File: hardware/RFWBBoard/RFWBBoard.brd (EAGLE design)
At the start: 90 x 56 mm, 123 parts, among them IC1 24LC025ST, J1 CON-71742-3003-BOT, M1 MOUNT-HOLE3.3, M2 MOUNT-HOLE3.3, M3 MOUNT-HOLE3.3, M4 MOUNT-HOLE3.3, M5 FIDUCIAL1X2, M6 FIDUCIAL1X2, M7 FIDUCIAL1X2, M8 FIDUCIAL1X2, U1 MAX2830IPC-7351, U2 LDB212G4010C-001, U3 LDB212G4010C-001, U4 AD8132MSOP8, U5 AD8132MSOP8, U6 AD8132MSOP8, U7 AD8132MSOP8, U8 ICS83021I, U9 ICS85320I, X1 SMA-SMD, X2 SMA-SMD, X3 FOX924B, X4 SMA-SMD, X5 SMA-SMD, X6 SMA-SMD, X7 SMA-SMD

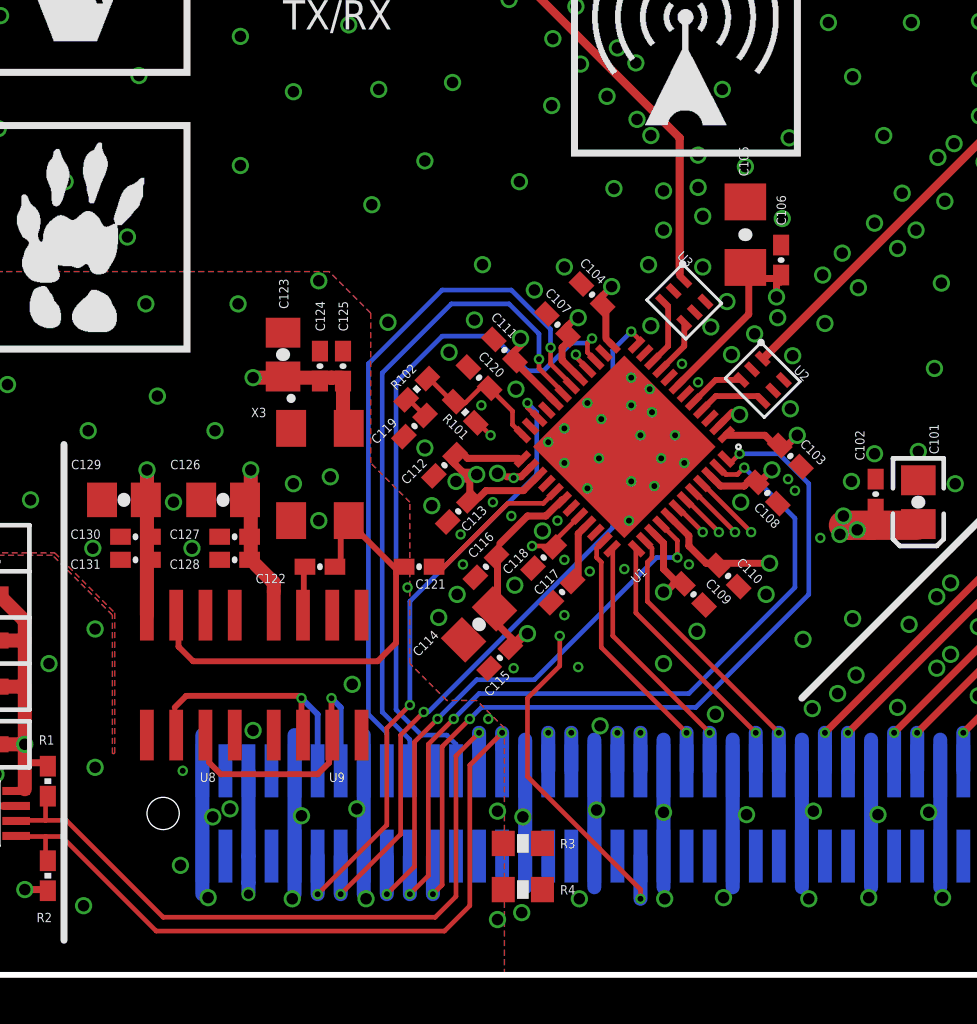
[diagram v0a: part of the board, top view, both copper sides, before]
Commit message: Errors corrected:
Radio Board

- External TCXO is connected to MAX2830 XTAL pin (28) instead of CTUNE pin (29)
- TCXO power supply digital, ground analog
- Mark for 1. pin for baluns not visible enough
- C105, C106 names covered by vias in documentation (PCB changed only)


Breakout Board

- 84 mezzanine connectors on top and bottom swapped


Power Board

- Silkscreen labels D1V5 and D3V3 are swapped
- VBUS measurement point not assembled
- SW2 name missing, needs caption (silk screen)
- Power input needs description (silk screen)
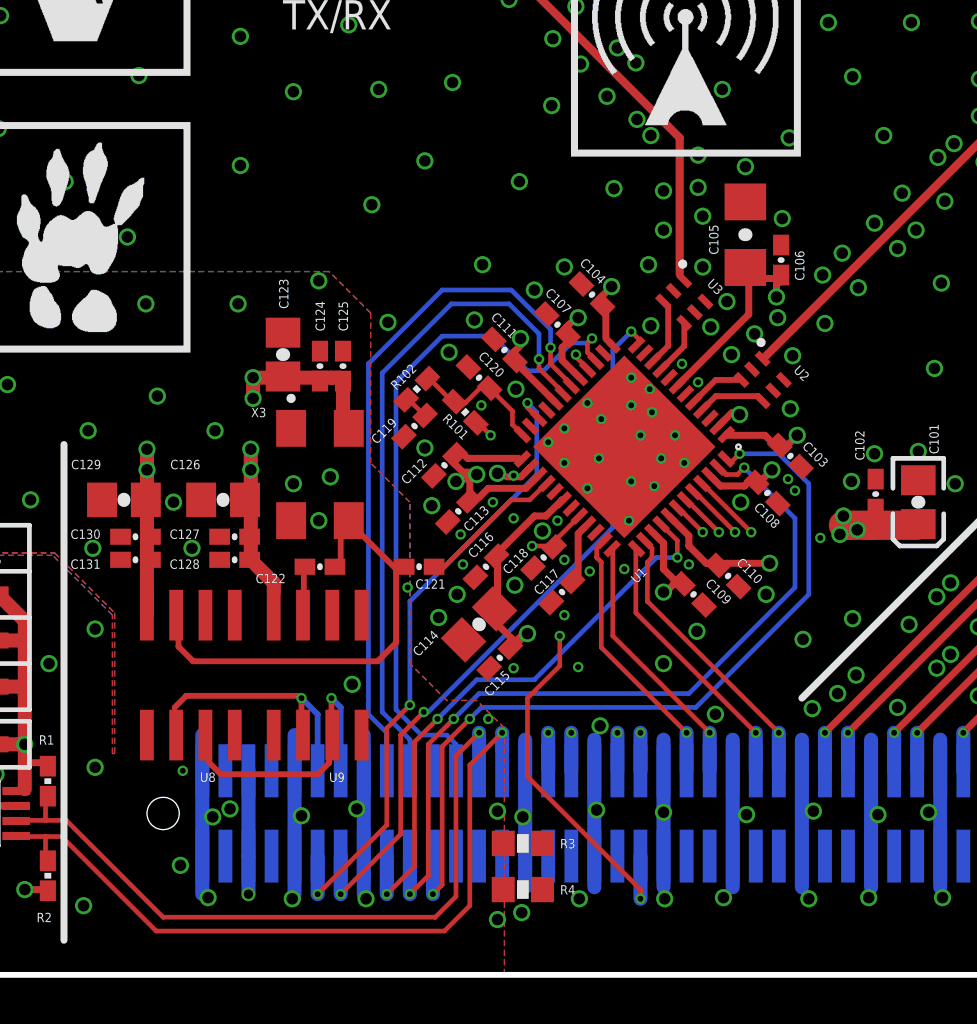
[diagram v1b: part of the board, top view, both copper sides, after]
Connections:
- net A3V3: no longer C123.1, C124.1, C125.1, C126.1, C127.1, C128.1, C129.1, C130.1, C131.1, U8.8, U9.8, X3.4
- net D3V3: now also C123.1, C124.1, C125.1, C126.1, C127.1, C128.1, C129.1, C130.1, C131.1, U8.8, U9.8, X3.4
- net N$6: now also U1.28; no longer U1.29
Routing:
- net D3V3: track 39.0 -> 81.6 mm, vias 3 -> 9
- net A3V3: track 134.4 -> 98.8 mm, vias 35 -> 32
- net DGND: vias 52 -> 51
- added copper zone on layer 15, net D3V3

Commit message: - Fiducials in both sides
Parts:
- added M10, M11, M12, M9: FIDUCIAL1X2, RFWBBoard:FIDUCIAL-1X2
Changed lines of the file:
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@@
 <grid distance="0.5" unitdist="mm" unit="mm" style="dots" multiple="1" display="yes" altdistance="0.1" altunitdist="mm" altunit="mm"/>
 <layers>
-<layer number="1" name="SIGNAL1" color="4" fill="1" visible="yes" active="yes"/>
+<layer number="1" name="SIGNAL1" color="4" fill="1" visible="no" active="yes"/>
 <layer number="2" name="GND1" color="2" fill="1" visible="no" active="yes"/>
-<layer number="3" name="SIGNAL2" color="4" fill="1" visible="yes" active="yes"/>
+<layer number="3" name="SIGNAL2" color="4" fill="1" visible="no" active="yes"/>
 <layer number="14" name="GND2" color="2" fill="1" visible="no" active="yes"/>
 <layer number="15" name="SUPPLY" color="14" fill="1" visible="no" active="yes"/>
@@
 <layer number="19" name="Unrouted" color="6" fill="1" visible="yes" active="yes"/>
 <layer number="20" name="Dimension" color="15" fill="1" visible="yes" active="yes"/>
-<layer number="21" name="tPlace" color="7" fill="1" visible="yes" active="yes"/>
+<layer number="21" name="tPlace" color="7" fill="1" visible="no" active="yes"/>
 <layer number="22" name="bPlace" color="7" fill="1" visible="no" active="yes"/>
 <layer number="23" name="tOrigins" color="15" fill="1" visible="no" active="yes"/>
-<layer number="24" name="bOrigins" color="15" fill="1" visible="no" active="yes"/>
-<layer number="25" name="tNames" color="4" fill="1" visible="yes" active="yes"/>
+<layer number="24" name="bOrigins" color="15" fill="1" visible="yes" active="yes"/>
+<layer number="25" name="tNames" color="4" fill="1" visible="no" active="yes"/>
 <layer number="26" name="bNames" color="1" fill="1" visible="no" active="yes"/>
 <layer number="27" name="tValues" color="7" fill="1" visible="no" active="yes"/>
 <layer number="28" name="bValues" color="7" fill="1" visible="no" active="yes"/>
-<layer number="29" name="tStop" color="7" fill="3" visible="yes" active="yes"/>
+<layer number="29" name="tStop" color="7" fill="3" visible="no" active="yes"/>
 <layer number="30" name="bStop" color="7" fill="6" visible="no" active="yes"/>
 <layer number="31" name="tCream" color="7" fill="4" visible="no" active="yes"/>
@@
 <attribute name="VALUE" x="90.715" y="21.825" size="1.27" layer="27" rot="R90"/>
 </element>
-<element name="M5" library="RFWBBoard" package="FIDUCIAL-1X2" value="FIDUCIAL1X2" x="2" y="2"/>
-<element name="M6" library="RFWBBoard" package="FIDUCIAL-1X2" value="FIDUCIAL1X2" x="2" y="48"/>
-<element name="M7" library="RFWBBoard" package="FIDUCIAL-1X2" value="FIDUCIAL1X2" x="88" y="48"/>
-<element name="M8" library="RFWBBoard" package="FIDUCIAL-1X2" value="FIDUCIAL1X2" x="88" y="2"/>
+<element name="M5" library="RFWBBoard" package="FIDUCIAL-1X2" value="FIDUCIAL1X2" x="2" y="2" locked="yes"/>
+<element name="M6" library="RFWBBoard" package="FIDUCIAL-1X2" value="FIDUCIAL1X2" x="2" y="48" locked="yes"/>
+<element name="M7" library="RFWBBoard" package="FIDUCIAL-1X2" value="FIDUCIAL1X2" x="88" y="48" locked="yes"/>
+<element name="M8" library="RFWBBoard" package="FIDUCIAL-1X2" value="FIDUCIAL1X2" x="88" y="2" locked="yes"/>
 <element name="U8" library="RFWBBoard" package="SOIC8" value="ICS83021I" x="24" y="13" smashed="yes">
 <attribute name="NAME" x="24.395" y="8.367" size="0.4064" layer="25"/>
@@
 <element name="LOGO6" library="Logo" package="LOGO-MARMOTE-10MM-SILKSCREEN" value="LOGO-MARMOTE-600MIL-10MM-SS" x="14" y="27"/>
 <element name="LOGO7" library="Logo" package="LOGO-RADIO-FILLED-10MM-SILKSCREEN" value="LOGO-RADIO-3-600MIL-10MM-SS" x="40.5" y="35.5"/>
+<element name="M9" library="RFWBBoard" package="FIDUCIAL-1X2" value="FIDUCIAL1X2" x="2" y="48" locked="yes" rot="MR0"/>
+<element name="M10" library="RFWBBoard" package="FIDUCIAL-1X2" value="FIDUCIAL1X2" x="88" y="48" locked="yes" rot="MR0"/>
+<element name="M11" library="RFWBBoard" package="FIDUCIAL-1X2" value="FIDUCIAL1X2" x="2" y="2" locked="yes" rot="MR0"/>
+<element name="M12" library="RFWBBoard" package="FIDUCIAL-1X2" value="FIDUCIAL1X2" x="88" y="2" locked="yes" rot="MR0"/>
 </elements>
 <signals>

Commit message: - Main Board: Only 4 DGND pins left out of 6 on mezzanine (2 became IO pins) - Power Board: Only 4 DGND pins left out of 6 on mezzanine (2 became IO pins) - RF Board: Only 4 DGND pins left out of 6 on mezzanine (2 became IO pins), initial changes in GPIOs
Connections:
- new net B1: U1.23
- new net B2: U1.11
- new net B3: U1.8
- new net B4: U1.34
- new net B5: U1.14
- new net B6: U1.3
- new net B7: U1.6
- net !SHDN: no longer J1.13
- net ANTSEL: no longer J1.19
- net DGND: no longer J1.15, J1.16
- net LD: no longer J1.11
- net RXHP: no longer J1.17
- net RXTX: no longer J1.21
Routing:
- net DGND: track 20.7 -> 13.8 mm
- net !SHDN: track 32.2 -> 30.5 mm
- net RXTX: track 36.0 -> 34.4 mm
- net RXHP: track 25.2 -> 23.5 mm
- net LD: track 27.9 -> 26.3 mm
- net ANTSEL: track 34.7 -> 33.0 mm
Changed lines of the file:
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@@
 <layer number="19" name="Unrouted" color="6" fill="1" visible="yes" active="yes"/>
 <layer number="20" name="Dimension" color="15" fill="1" visible="yes" active="yes"/>
-<layer number="21" name="tPlace" color="7" fill="1" visible="no" active="yes"/>
-<layer number="22" name="bPlace" color="7" fill="1" visible="no" active="yes"/>
-<layer number="23" name="tOrigins" color="15" fill="1" visible="no" active="yes"/>
+<layer number="21" name="tPlace" color="7" fill="1" visible="yes" active="yes"/>
+<layer number="22" name="bPlace" color="7" fill="1" visible="yes" active="yes"/>
+<layer number="23" name="tOrigins" color="15" fill="1" visible="yes" active="yes"/>
 <layer number="24" name="bOrigins" color="15" fill="1" visible="yes" active="yes"/>
 <layer number="25" name="tNames" color="4" fill="1" visible="no" active="yes"/>
@@
 <via x="23.55" y="4.75" extent="1-16" drill="0.5"/>
 <via x="23.65" y="8.85" extent="1-16" drill="0.254"/>
-<contactref element="J1" pad="16"/>
 <contactref element="J1" pad="10"/>
-<contactref element="J1" pad="15"/>
 <contactref element="J1" pad="9"/>
 <polygon width="0.254" layer="15" rank="2">
@@
 <wire x1="24.5" y1="3.5" x2="24.5" y2="10.4" width="0.6096" layer="16"/>
 <wire x1="28.5" y1="3.5" x2="28.5" y2="10.4" width="0.6096" layer="16"/>
-<wire x1="31.5" y1="3.5" x2="31.5" y2="10.4" width="0.6096" layer="16"/>
 <via x="36.9" y="11.1" extent="1-16" drill="0.254"/>
 <via x="33.4" y="16.8" extent="1-16" drill="0.254"/>
@@
 <contactref element="U1" pad="22"/>
 <via x="29.5" y="3.5" extent="1-16" drill="0.254"/>
-<contactref element="J1" pad="11"/>
-<wire x1="29.5" y1="5.15" x2="29.5" y2="3.5" width="0.6096" layer="16"/>
 <wire x1="38.9" y1="24.3" x2="39.0876875" y2="24.137434375" width="0.2032" layer="1"/>
 </signal>
@@
 <via x="34.7" y="11.1" extent="1-16" drill="0.254"/>
 <via x="32.5" y="3.5" extent="1-16" drill="0.254"/>
-<contactref element="J1" pad="17"/>
-<wire x1="32.5" y1="5.15" x2="32.5" y2="3.5" width="0.6096" layer="16"/>
 </signal>
 <signal name="ANTSEL">
@@
 <via x="35.4" y="11.1" extent="1-16" drill="0.254"/>
 <via x="33.5" y="3.5" extent="1-16" drill="0.254"/>
-<contactref element="J1" pad="19"/>
-<wire x1="33.5" y1="5.15" x2="33.5" y2="3.5" width="0.6096" layer="16"/>
 <wire x1="46.8658625" y1="22.016115625" x2="47.1" y2="21.8" width="0.2032" layer="1"/>
 </signal>
@@
 <via x="36.1" y="11.1" extent="1-16" drill="0.254"/>
 <via x="34.5" y="3.5" extent="1-16" drill="0.254"/>
-<contactref element="J1" pad="21"/>
-<wire x1="34.5" y1="5.15" x2="34.5" y2="3.5" width="0.6096" layer="16"/>
 <wire x1="47.219415625" y1="22.36966875" x2="47.4" y2="22.2" width="0.2032" layer="1"/>
 </signal>
@@
 <via x="43.1" y="27.9" extent="1-16" drill="0.254"/>
 <via x="34.1" y="11.4" extent="1-16" drill="0.254"/>
-<contactref element="J1" pad="13"/>
-<wire x1="30.5" y1="5.15" x2="30.5" y2="3.5" width="0.6096" layer="16"/>
 <wire x1="43.330328125" y1="27.319415625" x2="43.5" y2="27.5" width="0.2032" layer="1"/>
 </signal>
@@
 </polygon>
 </signal>
+<signal name="B1">
+<contactref element="U1" pad="23"/>
+</signal>
+<signal name="B2">
+<contactref element="U1" pad="11"/>
+</signal>
+<signal name="B3">
+<contactref element="U1" pad="8"/>
+</signal>
+<signal name="B4">
+<contactref element="U1" pad="34"/>
+</signal>
+<signal name="B5">
+<contactref element="U1" pad="14"/>
+</signal>
+<signal name="B6">
+<contactref element="U1" pad="3"/>
+</signal>
+<signal name="B7">
+<contactref element="U1" pad="6"/>
+</signal>
 </signals>

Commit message: - B1-B7 vias
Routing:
- net B5: track 0.00 -> 0.91 mm, vias 0 -> 1
- net B7: track 0.00 -> 0.90 mm, vias 0 -> 1
- net B6: track 0.00 -> 0.88 mm, vias 0 -> 1
- net B4: track 0.00 -> 0.88 mm, vias 0 -> 1
- net B2: track 0.00 -> 0.85 mm, vias 0 -> 1
- net B1: track 0.00 -> 0.84 mm, vias 0 -> 1
- net B3: track 0.00 -> 0.82 mm, vias 0 -> 1
- net !CS: track 30.3 -> 29.6 mm
- net DGND: vias 51 -> 50

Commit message: - TCXO + XTAL footprint - 1ppm SMA - Parallel gain control - Routing - Schematic updated with switches
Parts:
- removed C122: 1000pF, RFWBBoard:C0402
- removed C129: 10uF, RFWBBoard:C0805
- removed C130: 100nF, RFWBBoard:C0402
- removed C131: 100pF, RFWBBoard:C0402
- removed U8: ICS83021I, RFWBBoard:SOIC8
- removed U9: ICS85320I, RFWBBoard:SOIC8
- added R5, R6, R7, R8: 0, RFWBBoard:R0402
- added R9: 0, RFWBBoard:R0603
- added SW1, SW2, SW3, SW4: SWITCH-CJS-1200TA, RFWBBoard:SWITCH-DIP-CJS
- added X8: SMA-SMD, RFWBBoard:SMA-SMD
- added X9: CX3225SB, RFWBBoard:CX3225SB
- C126: value 10uF -> 18pF; device RFWBBoard:C0805 -> RFWBBoard:C0402
- C127: value 100nF -> 33pF
- C128: value 100pF -> 1000pF
- moved LOGO6 32.5 mm to (12.5, 59.5)
- moved LOGO4 32.5 mm to (1.00, 59.5)
- moved C126 10.6 mm to (33.3, 13.6), turned to 90 degrees
- moved C127 7.78 mm to (33.3, 16.6), turned to 90 degrees
- moved C128 5.47 mm to (31.3, 17.1), turned to 0 degrees
- moved C124 2.28 mm to (28.7, 24.3)
- moved C125 2.28 mm to (29.7, 24.3)
- moved C123 2.28 mm to (27.1, 24.8)
- moved C121 1.99 mm to (33.3, 19.6), turned to 90 degrees
- moved X3 1.41 mm to (29.4, 20.3), turned to 0 degrees
- moved C114 0.22 mm to (36.7, 15.1)
- moved C115 0.22 mm to (37.6, 13.7)
- moved C116 0.22 mm to (37.0, 17.6)
- moved C117 0.10 mm to (40.1, 16.5)
- moved C118 0.10 mm to (39.3, 18.0)
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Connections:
- new net A3V3_BB: C41.+, C42.1, C43.1, C51.+, C52.1, C53.1, C61.+, C62.1, C63.1, C71.+, C72.1, C73.1, R451.2, R671.2, R8.2, U4.3, U5.3, U6.3, U7.3
- new net A3V3_RF: C101.+, C102.1, C103.1, C104.1, C105.2, C106.2, C107.1, C108.1, C109.1, C110.1, C111.1, C112.1, C113.1, C114.1, C115.1, C116.1, R9.2, U1.1, U1.13, U1.17, U1.20, U1.25, U1.27, U1.30, U1.39, U1.41, U1.46, U1.7
- new net N$37: C123.1, C124.1, C125.1, R7.1, X3.4
- new net N$38: R5.2, U1.21
- new net N$40: C126.2, C127.1, U1.29
- net !SHDN: now also J1.13
- net A3V3: now also R8.1, R9.1; no longer C101.+, C102.1, C103.1, C104.1, C105.2, C106.2, C107.1, C108.1, C109.1, C110.1, C111.1, C112.1, C113.1, C114.1, C115.1, C116.1, C41.+, C42.1, C43.1, C51.+, C52.1, C53.1, C61.+, C62.1, C63.1, C71.+, C72.1, C73.1, R451.2, R671.2, U1.1, U1.13, U1.17, U1.20, U1.25, U1.27, U1.30, U1.39, U1.41, U1.46, U1.7, U4.3, U5.3, U6.3, U7.3
- net ANTSEL: now also SW2.2
- net B1: now also J1.15
- net B2: now also J1.19
- net B3: now also J1.17
- net B4: now also J1.23
- net B5: now also J1.16
- net B6: now also SW3.2
- net B7: now also SW4.2
- net CLK1: now also X8.1; no longer U8.2, U9.2
- net CLK2: now also R5.1, R6.1; no longer U8.3, U9.3
- net D3V3: now also R7.2, SW1.1, SW2.1, SW3.1, SW4.1; no longer C123.1, C124.1, C125.1, C126.1, C127.1, C128.1, C129.1, C130.1, C131.1, U8.8, U9.8, X3.4
- net DGND: now also C126.1, SW1.3, SW2.3, SW3.3, SW4.3, X8.2@1, X8.2@2, X8.2@3, X8.2@4, X8.2@5, X8.2@6, X9.1, X9.2, X9.4; no longer C126.2, C127.2, C128.2, C129.2, C130.2, C131.2, U8.5, U9.5
- net LD: now also J1.11
- net N$36: now also R6.2; no longer C122.2, U8.7
- net N$39: now also C128.1, X9.3; no longer C122.1, U9.7
- net N$6: now also C127.2, C128.2
- net RXHP: now also SW1.2
- net RXTX: now also J1.21
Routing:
- net A3V3: track 98.9 -> 7.20 mm, vias 32 -> 4
- net A3V3_RF: track 0.00 -> 61.1 mm, vias 0 -> 11
- net D3V3: track 81.6 -> 38.9 mm, vias 9 -> 4
- net B6: track 0.88 -> 37.1 mm
- net B7: track 0.90 -> 34.5 mm
- net A3V3_BB: track 0.00 -> 30.5 mm, vias 0 -> 14
- net B3: track 0.82 -> 26.0 mm, vias 1 -> 2
- net B5: track 0.91 -> 25.5 mm, vias 1 -> 3
- net N$38: track 0.00 -> 20.3 mm, vias 0 -> 2
- net B2: track 0.85 -> 20.4 mm, vias 1 -> 2
- net RXHP: track 23.5 -> 41.7 mm, vias 3 -> 1
- net B1: track 0.84 -> 17.4 mm, vias 1 -> 2
- net CLK2: track 13.4 -> 1.65 mm
- net !SHDN: track 30.8 -> 20.4 mm, vias 3 -> 2
- net N$40: track 0.00 -> 9.92 mm
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- added copper zone on layer 15, net A3V3_BB
- added copper zone on layer 15, net A3V3_RF

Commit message: - RF board routing done
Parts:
- removed R3: DNP, RFWBBoard:R0603
- R4, R9: device RFWBBoard:R0603 -> RFWBBoard:R1206
- R7, R8: device RFWBBoard:R0402 -> RFWBBoard:R1206
- moved LOGO4 76.9 mm to (51.5, 1.50)
- moved LOGO5 46.2 mm to (41.0, 1.50)
- moved LOGO6 17.5 mm to (12.5, 42.0)
- moved SW1 9.00 mm to (16.5, 27.5)
- moved R7 7.13 mm to (24.6, 21.6), turned to 270 degrees
- moved SW3 4.50 mm to (12.0, 27.5)
- moved SW4 4.50 mm to (7.50, 27.5)
- moved R8 1.84 mm to (63.1, 7.90)
- moved C124 1.33 mm to (30.0, 24.0)
- moved C101 1.17 mm to (55.1, 19.4), turned to 45 degrees
- moved R4 0.85 mm to (39.2, 3.40), turned to 90 degrees
- moved R9 0.81 mm to (51.8, 16.1), turned to 45 degrees
- moved C125 0.76 mm to (29.0, 24.0)
- moved C123 0.42 mm to (27.4, 24.5)
- moved C102 0.22 mm to (53.8, 20.6), turned to 45 degrees
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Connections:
- net !SHDN: now also J1.17; no longer J1.13
- net AGND: no longer R3.2
- net B1: now also J1.11; no longer J1.15
- net B3: now also J1.21; no longer J1.17
- net B4: now also J1.15; no longer J1.23
- net DGND: no longer R3.1
- net LD: now also J1.13; no longer J1.11
- net RXTX: now also J1.23; no longer J1.21
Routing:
- net B7: track 34.5 -> 48.4 mm, vias 1 -> 2
- net B2: track 20.4 -> 31.9 mm, vias 2 -> 3
- net B4: track 10.6 -> 22.0 mm, vias 2 -> 3
- net !SHDN: track 20.4 -> 31.4 mm, vias 2 -> 3
- net D3V3: track 38.9 -> 49.6 mm, vias 4 -> 16
- net B1: track 17.4 -> 27.3 mm, vias 2 -> 3
- net B6: track 37.1 -> 46.5 mm, vias 1 -> 2
- net LD: track 18.2 -> 27.6 mm, vias 2 -> 3
- net B3: track 26.0 -> 33.8 mm, vias 2 -> 3
- net RXTX: track 24.5 -> 32.1 mm, vias 2 -> 3
- net N$37: track 0.00 -> 7.06 mm
- net A3V3_RF: track 61.1 -> 67.9 mm, vias 11 -> 26
- net B5: track 25.5 -> 32.2 mm, vias 3 -> 1
- net A3V3_BB: track 30.5 -> 36.1 mm, vias 14 -> 21
- net RXHP: track 41.7 -> 45.9 mm, vias 1 -> 2
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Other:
- board text added: "ANTSEL"
- board text added: "B6"
- board text added: "B7"
- board text added: "RXHP"

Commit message: - BOM updated - pull down resistor for SHDN - Names arranged
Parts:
- removed X3: FOX924B, RFWBBoard:FOX924
- removed X9: CX3225SB, RFWBBoard:CX3225SB
- added J2, J3: SMA-SMD, RFWBBoard:SMA-SMD
- added R10: 30k, RFWBBoard:R0402
- R41, R51: value 49.9 -> 10k
- R42, R52: value 24.9 -> 10k
- R43, R44, R53, R54: value 348 -> 1.58k
- R45, R46, R55, R56: value 348 -> 1.3k
- RA00, RA10, RA20, RA21, RWP0: value DNP -> 0
- X1: value SMA-SMD -> CX3225SB; device RFWBBoard:SMA-SMD -> RFWBBoard:CX3225SB
- X2: value SMA-SMD -> FOX924B; device RFWBBoard:SMA-SMD -> RFWBBoard:FOX924
- moved X1 43.4 mm to (30.7, 14.3), turned to 90 degrees
- moved LOGO5 31.8 mm to (25.0, 29.0)
- moved X2 26.9 mm to (29.4, 20.3), turned to 0 degrees
- moved LOGO4 7.50 mm to (44.0, 1.50)
- renumbered X4 to J4, X5 to J5, X6 to J6, X7 to J7, X8 to J8
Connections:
- net CLK1 renamed CLK_EXT
- net CLK2 renamed CLK_LOC
- net !SHDN: now also R10.1
- net AGND: now also J2.2@1, J2.2@2, J2.2@3, J2.2@4, J2.2@5, J2.2@6, J3.2@1, J3.2@2, J3.2@3, J3.2@4, J3.2@5, J3.2@6; no longer X1.2@1, X1.2@2, X1.2@3, X1.2@4, X1.2@5, X1.2@6, X2.2@1, X2.2@2, X2.2@3, X2.2@4, X2.2@5, X2.2@6
- net DGND: now also R10.2, X1.1, X1.2, X1.4, X2.2; no longer X3.2, X9.1, X9.2, X9.4
- net N$36: now also X2.3; no longer X3.3
- net N$37: now also X2.4; no longer X3.4
- net N$39: now also X1.3; no longer X9.3
- net N$8: now also J2.1; no longer X1.1
- net N$9: now also J3.1; no longer X2.1
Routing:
- net D3V3: track 49.6 -> 48.3 mm
- net !SHDN: track 31.4 -> 32.7 mm
- net I2C_SDA: vias 1 -> 3
- net I2C_SCL: vias 1 -> 3
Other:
- board text added: "Copyright c 2013"
- board text removed: "Copyright c 2012"
